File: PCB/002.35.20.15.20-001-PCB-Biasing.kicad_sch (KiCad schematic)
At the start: 7 parts

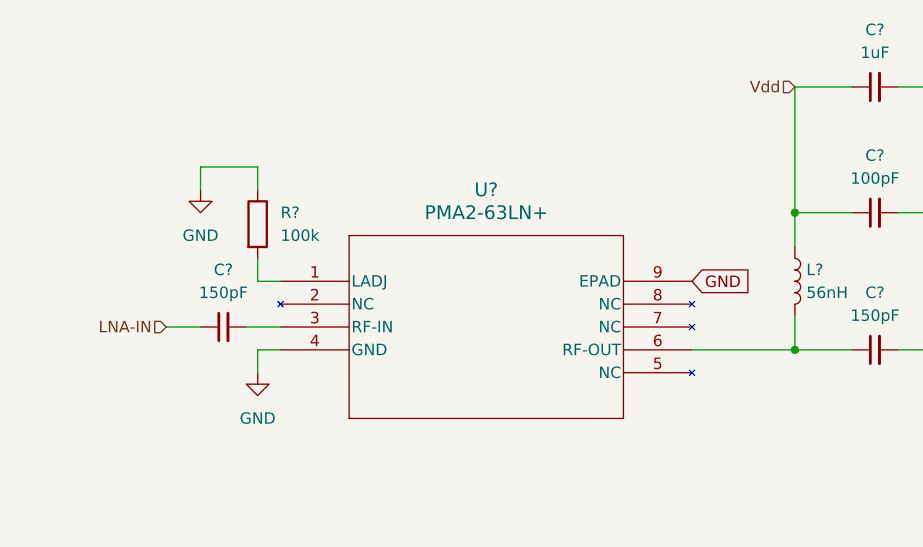
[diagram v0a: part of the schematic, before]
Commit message: PCB Rev B complete: compacted board and fixed sma pads
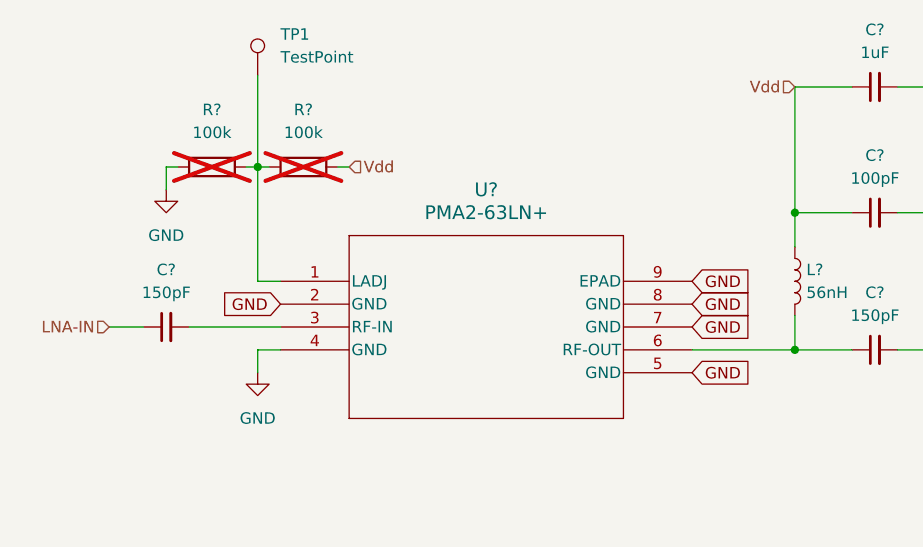
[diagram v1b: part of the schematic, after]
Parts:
- added R?: 100k, Resistor_SMD:R_0402_1005Metric, symbol Device:R
- added TP1: TestPoint, TestPoint:TestPoint_Loop_D2.54mm_Drill1.5mm_Beaded, symbol Connector:TestPoint
- R?: now not fitted
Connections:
- net GND: now also U?.2 (GND), U?.5 (GND), U?.7 (GND), U?.8 (GND)
- net Vdd: now also R?.2
- net at R?.2, U?.1 (LADJ): now also R?.1, TP1.1
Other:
- moved on the sheet: C?
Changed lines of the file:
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@@
   (junction (at 181.61 113.03) (diameter 0) (color 0 0 0 0)
   )
+  (junction (at 121.92 92.71) (diameter 0) (color 0 0 0 0)
+  )
   (wire (pts (xy 193.04 83.82) (xy 196.85 83.82))
     (stroke (width 0) (type default))
   )
-  (wire (pts (xy 115.57 92.71) (xy 115.57 95.25))
-    (stroke (width 0) (type default))
-  )
-  (wire (pts (xy 111.76 110.49) (xy 115.57 110.49))
+  (wire (pts (xy 105.41 110.49) (xy 109.22 110.49))
+    (stroke (width 0) (type default))
+  )
+  (wire (pts (xy 111.76 92.71) (xy 111.76 95.25))
+    (stroke (width 0) (type default))
+  )
+  (wire (pts (xy 121.92 82.55) (xy 121.92 92.71))
     (stroke (width 0) (type default))
   )
@@
     (stroke (width 0) (type default))
   )
-  (wire (pts (xy 120.65 110.49) (xy 124.46 110.49))
+  (wire (pts (xy 114.3 110.49) (xy 124.46 110.49))
     (stroke (width 0) (type default))
   )
@@
     (stroke (width 0) (type default))
   )
-  (wire (pts (xy 121.92 95.25) (xy 121.92 92.71))
-    (stroke (width 0) (type default))
-  )
   (wire (pts (xy 124.46 105.41) (xy 121.92 105.41))
     (stroke (width 0) (type default))
   )
+  (wire (pts (xy 123.19 92.71) (xy 121.92 92.71))
+    (stroke (width 0) (type default))
+  )
   (wire (pts (xy 187.96 97.79) (xy 181.61 97.79))
     (stroke (width 0) (type default))
@@
     (stroke (width 0) (type default))
   )
+  (wire (pts (xy 120.65 92.71) (xy 121.92 92.71))
+    (stroke (width 0) (type default))
+  )
+  (wire (pts (xy 113.03 92.71) (xy 111.76 92.71))
+    (stroke (width 0) (type default))
+  )
   (wire (pts (xy 193.04 97.79) (xy 196.85 97.79))
     (stroke (width 0) (type default))
   )
-  (wire (pts (xy 121.92 92.71) (xy 115.57 92.71))
-    (stroke (width 0) (type default))
-  )
-  (wire (pts (xy 121.92 105.41) (xy 121.92 102.87))
+  (wire (pts (xy 132.08 92.71) (xy 130.81 92.71))
+    (stroke (width 0) (type default))
+  )
+  (wire (pts (xy 121.92 92.71) (xy 121.92 105.41))
     (stroke (width 0) (type default))
   )
@@
   (text "LNA Biasing Circuit" (at 186.69 190.5 0)
     (effects (font (size 1.27 1.27)) (justify left bottom))
+  )
+  (global_label "GND" (shape input) (at 170.18 110.49 0) (fields_autoplaced)
+    (effects (font (size 1.27 1.27)) (justify left))
+    (property "Intersheetrefs" "${INTERSHEET_REFS}" (at 176.9563 110.49 0)
+      (effects (font (size 1.27 1.27)) (justify left) hide)
+    )
   )
   (global_label "GND" (shape input) (at 170.18 105.41 0) (fields_autoplaced)
@@
     )
   )
+  (global_label "GND" (shape input) (at 124.46 107.95 180) (fields_autoplaced)
+    (effects (font (size 1.27 1.27)) (justify right))
+    (property "Intersheetrefs" "${INTERSHEET_REFS}" (at 117.6837 107.95 0)
+      (effects (font (size 1.27 1.27)) (justify right) hide)
+    )
+  )
+  (global_label "GND" (shape input) (at 170.18 115.57 0) (fields_autoplaced)
+    (effects (font (size 1.27 1.27)) (justify left))
+    (property "Intersheetrefs" "${INTERSHEET_REFS}" (at 176.9563 115.57 0)
+      (effects (font (size 1.27 1.27)) (justify left) hide)
+    )
+  )
+  (global_label "GND" (shape input) (at 170.18 107.95 0) (fields_autoplaced)
+    (effects (font (size 1.27 1.27)) (justify left))
+    (property "Intersheetrefs" "${INTERSHEET_REFS}" (at 176.9563 107.95 0)
+      (effects (font (size 1.27 1.27)) (justify left) hide)
+    )
+  )
   (hierarchical_label "LNA-OUT" (shape input) (at 196.85 113.03 0) (fields_autoplaced)
     (effects (font (size 1.27 1.27)) (justify left))
   )
-  (hierarchical_label "LNA-IN" (shape input) (at 111.76 110.49 180) (fields_autoplaced)
+  (hierarchical_label "Vdd" (shape input) (at 132.08 92.71 0) (fields_autoplaced)
+    (effects (font (size 1.27 1.27)) (justify left))
+  )
+  (hierarchical_label "LNA-IN" (shape input) (at 105.41 110.49 180) (fields_autoplaced)
     (effects (font (size 1.27 1.27)) (justify right))
   )
@@
     )
   )
-  (symbol (lib_id "power:GND") (at 115.57 95.25 0) (unit 1)
-    (in_bom yes) (on_board yes) (dnp no) (fields_autoplaced)
-    (property "Reference" "#PWR?" (at 115.57 101.6 0)
-      (effects (font (size 1.27 1.27)) hide)
-    )
-    (property "Value" "GND" (at 115.57 100.33 0)
-      (effects (font (size 1.27 1.27)))
-    )
-    (property "Footprint" "" (at 115.57 95.25 0)
-      (effects (font (size 1.27 1.27)) hide)
-    )
-    (property "Datasheet" "" (at 115.57 95.25 0)
+  (symbol (lib_id "power:GND") (at 111.76 95.25 0) (unit 1)
+    (in_bom yes) (on_board yes) (dnp no) (fields_autoplaced)
+    (property "Reference" "#PWR?" (at 111.76 101.6 0)
+      (effects (font (size 1.27 1.27)) hide)
+    )
+    (property "Value" "GND" (at 111.76 100.33 0)
+      (effects (font (size 1.27 1.27)))
+    )
+    (property "Footprint" "" (at 111.76 95.25 0)
+      (effects (font (size 1.27 1.27)) hide)
+    )
+    (property "Datasheet" "" (at 111.76 95.25 0)
       (effects (font (size 1.27 1.27)) hide)
     )
@@
     )
   )
-  (symbol (lib_id "Device:C_Small") (at 118.11 110.49 90) (unit 1)
-    (in_bom yes) (on_board yes) (dnp no) (fields_autoplaced)
-    (property "Reference" "C?" (at 118.1163 104.14 90)
-      (effects (font (size 1.27 1.27)))
-    )
-    (property "Value" "150pF" (at 118.1163 106.68 90)
-      (effects (font (size 1.27 1.27)))
-    )
-    (property "Footprint" "Capacitor_SMD:C_0402_1005Metric" (at 118.11 110.49 0)
-      (effects (font (size 1.27 1.27)) hide)
-    )
-    (property "Datasheet" "~" (at 118.11 110.49 0)
+  (symbol (lib_id "Device:C_Small") (at 111.76 110.49 90) (unit 1)
+    (in_bom yes) (on_board yes) (dnp no) (fields_autoplaced)
+    (property "Reference" "C?" (at 111.7663 104.14 90)
+      (effects (font (size 1.27 1.27)))
+    )
+    (property "Value" "150pF" (at 111.7663 106.68 90)
+      (effects (font (size 1.27 1.27)))
+    )
+    (property "Footprint" "Capacitor_SMD:C_0402_1005Metric" (at 111.76 110.49 0)
+      (effects (font (size 1.27 1.27)) hide)
+    )
+    (property "Datasheet" "~" (at 111.76 110.49 0)
       (effects (font (size 1.27 1.27)) hide)
     )
@@
     )
   )
-  (symbol (lib_id "Device:R") (at 121.92 99.06 0) (unit 1)
-    (in_bom yes) (on_board yes) (dnp no) (fields_autoplaced)
-    (property "Reference" "R?" (at 124.46 97.79 0)
+  (symbol (lib_id "Connector:TestPoint") (at 121.92 82.55 0) (unit 1)
+    (in_bom yes) (on_board yes) (dnp no) (fields_autoplaced)
+    (property "Reference" "TP1" (at 124.46 77.978 0)
       (effects (font (size 1.27 1.27)) (justify left))
     )
-    (property "Value" "100k" (at 124.46 100.33 0)
+    (property "Value" "TestPoint" (at 124.46 80.518 0)
       (effects (font (size 1.27 1.27)) (justify left))
     )
-    (property "Footprint" "Resistor_SMD:R_0402_1005Metric" (at 120.142 99.06 90)
-      (effects (font (size 1.27 1.27)) hide)
-    )
-    (property "Datasheet" "~" (at 121.92 99.06 0)
+    (property "Footprint" "TestPoint:TestPoint_Loop_D2.54mm_Drill1.5mm_Beaded" (at 127 82.55 0)
+      (effects (font (size 1.27 1.27)) hide)
+    )
+    (property "Datasheet" "~" (at 127 82.55 0)
+      (effects (font (size 1.27 1.27)) hide)
+    )
+    (pin "1")
+    (instances
+      (project "002.35.20.15.20-001-PCB-LNA"
+        (path "/a33db424-96f2-4015-ba95-8b9f2330ef17/9ff85c99-1040-4eb9-b5d8-3cc01caa0e77"
+          (reference "TP1") (unit 1)
+        )
+        (path "/a33db424-96f2-4015-ba95-8b9f2330ef17/ba672304-1315-4178-9e1d-d553703e5b04"
+          (reference "TP2") (unit 1)
+        )
+      )
+    )
+  )
+  (symbol (lib_id "Device:R") (at 116.84 92.71 90) (unit 1)
+    (in_bom yes) (on_board yes) (dnp yes) (fields_autoplaced)
+    (property "Reference" "R?" (at 116.84 86.36 90)
+      (effects (font (size 1.27 1.27)))
+    )
+    (property "Value" "100k" (at 116.84 88.9 90)
+      (effects (font (size 1.27 1.27)))
+    )
+    (property "Footprint" "Resistor_SMD:R_0402_1005Metric" (at 116.84 94.488 90)
+      (effects (font (size 1.27 1.27)) hide)
+    )
+    (property "Datasheet" "~" (at 116.84 92.71 0)
       (effects (font (size 1.27 1.27)) hide)
     )
@@
         )
       )
+    )
+  )
+  (symbol (lib_id "Device:R") (at 127 92.71 90) (unit 1)
+    (in_bom yes) (on_board yes) (dnp yes) (fields_autoplaced)
+    (property "Reference" "R?" (at 127 86.36 90)
+      (effects (font (size 1.27 1.27)))
+    )
+    (property "Value" "100k" (at 127 88.9 90)
+      (effects (font (size 1.27 1.27)))
+    )
+    (property "Footprint" "Resistor_SMD:R_0402_1005Metric" (at 127 94.488 90)
+      (effects (font (size 1.27 1.27)) hide)
+    )
+    (property "Datasheet" "~" (at 127 92.71 0)
+      (effects (font (size 1.27 1.27)) hide)
+    )
+    (pin "1")
+    (pin "2")
+    (instances
+      (project "002.35.20.15.20-001-PCB-LNA"
+        (path "/a33db424-96f2-4015-ba95-8b9f2330ef17"
+          (reference "R?") (unit 1)
+        )
+        (path "/a33db424-96f2-4015-ba95-8b9f2330ef17/9ff85c99-1040-4eb9-b5d8-3cc01caa0e77"
+          (reference "R3") (unit 1)
+        )
+        (path "/a33db424-96f2-4015-ba95-8b9f2330ef17/ba672304-1315-4178-9e1d-d553703e5b04"
+          (reference "R4") (unit 1)
+        )
+      )

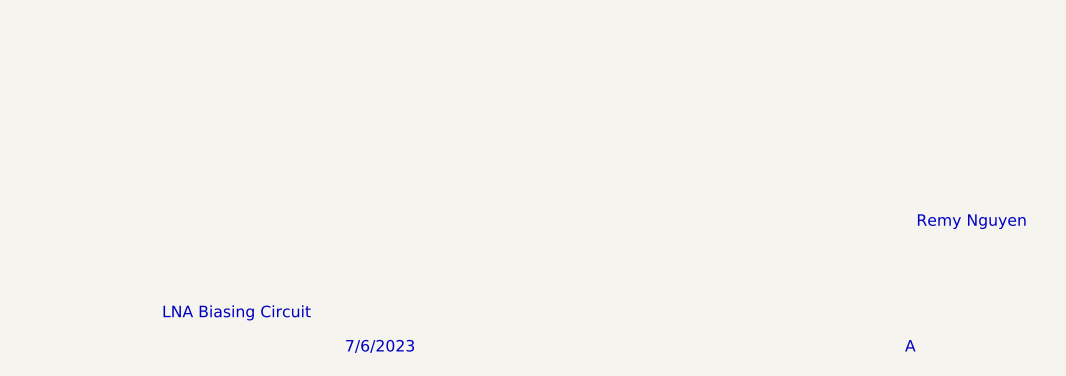
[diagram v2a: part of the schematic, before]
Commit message: Drawing sheets updated
* A4 --> Letter
* SMA connector diameter dimensioned
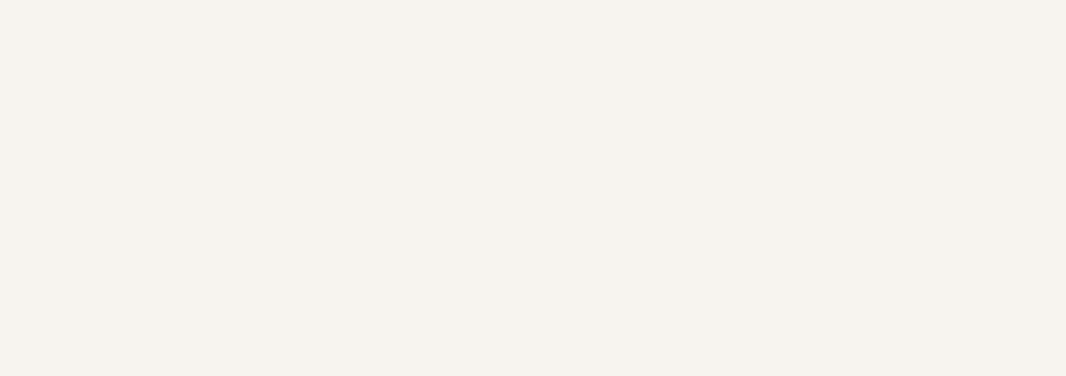
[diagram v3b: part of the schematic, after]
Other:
- note removed: "7/6/2023"
- note removed: "A"
- note removed: "LNA Biasing Circuit"
- note removed: "Remy Nguyen"
- company: (none) -> National Radio Astronomy Observatory
- title: (none) -> RF-DFS Gain Circuit
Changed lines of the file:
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@@
 (kicad_sch (version 20230121) (generator eeschema)
-  (paper "A4")
+  (paper "USLetter")
+  (title_block
+    (title "RF-DFS Gain Circuit")
+    (date "2/23/2024")
+    (rev "C")
+    (company "National Radio Astronomy Observatory")
+    (comment 1 "Remy Nguyen")
+  )
   (junction (at 181.61 97.79) (diameter 0) (color 0 0 0 0)
   )
@@
     (stroke (width 0) (type default))
   )
-  (text "Remy Nguyen" (at 270.51 180.34 0)
-    (effects (font (size 1.27 1.27)) (justify left bottom))
-  )
-  (text "A" (at 269.24 194.31 0)
-    (effects (font (size 1.27 1.27)) (justify left bottom))
-  )
-  (text "7/6/2023" (at 207.01 194.31 0)
-    (effects (font (size 1.27 1.27)) (justify left bottom))
-  )
-  (text "LNA Biasing Circuit" (at 186.69 190.5 0)
-    (effects (font (size 1.27 1.27)) (justify left bottom))
-  )
   (global_label "GND" (shape input) (at 170.18 110.49 0) (fields_autoplaced)
